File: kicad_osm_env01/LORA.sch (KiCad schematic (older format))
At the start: 12 parts

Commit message: kicad review sch initial
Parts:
- added TP?: Test_Point, TestPoint:TestPoint_THTPad_D1.0mm_Drill0.5mm, symbol OSM_env01-rescue:Test_Point-Connector-ESP32-EVB_Rev_D-rescue
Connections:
- net LORA_NRST: now reaches U?.18 (MCU_NRST)
- net LORA_NRST: now also TP?.1
- no-connect marks 14 -> 13
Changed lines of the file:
@@
 $Descr A4 11693 8268
 encoding utf-8
-Sheet 4 9
+Sheet 3 9
 Title ""
 Date ""
@@
 $EndComp
 Wire Wire Line
-	3300 3425 2950 3425
+	3300 3425 3250 3425
 Wire Wire Line
 	3300 3650 2950 3650
@@
 Text Label 2950 3650 0    50   ~ 0
 LORA_RX
-Text Label 2950 3425 0    50   ~ 0
-LORA_CTS
 Wire Wire Line
 	4000 2800 4275 2800
@@
 NoConn ~ 9025 3550
 NoConn ~ 9025 3425
-NoConn ~ 9025 3300
 NoConn ~ 7275 3550
 $Comp
@@
 Wire Wire Line
 	7275 3675 6900 3675
-Text Label 6900 3675 0    50   ~ 0
+Wire Wire Line
+	7275 3800 6900 3800
+Text HLabel 6900 3675 0    50   Input ~ 0
 LORA_RX
-Wire Wire Line
-	7275 3800 6900 3800
-Text Label 6900 3800 0    50   ~ 0
+Text HLabel 6900 3800 0    50   Input ~ 0
 LORA_TX
+Text HLabel 3175 3350 0    50   Input ~ 0
+LORA_CTS
+Wire Wire Line
+	3175 3350 3250 3350
+Wire Wire Line
+	3250 3350 3250 3425
+Connection ~ 3250 3425
+Wire Wire Line
+	3250 3425 2950 3425
+Text HLabel 9400 3300 2    50   Input ~ 0
+LORA_NRST
+Wire Wire Line
+	9400 3300 9300 3300
+$Comp
+L OSM_env01-rescue:Test_Point-Connector-ESP32-EVB_Rev_D-rescue TP?
+U 1 1 606B4551
+P 9300 3400
+AR Path="/606B4551" Ref="TP?"  Part="1"
+AR Path="/60880AD8/606B4551" Ref="TP?"  Part="1"
+F 0 "TP?" V 9300 4150 50  0000 C CNN
+F 1 "Test_Point" V 9300 3775 50  0000 C CNN
+F 2 "TestPoint:TestPoint_THTPad_D1.0mm_Drill0.5mm" H 9500 3400 50  0001 C CNN
+F 3 "~" H 9500 3400 50  0001 C CNN
+	1    9300 3400
+	0    1    -1   0
+$EndComp
+Wire Wire Line
+	9300 3400 9300 3300
+Connection ~ 9300 3300
+Wire Wire Line
+	9300 3300 9025 3300
 $EndSCHEMATC

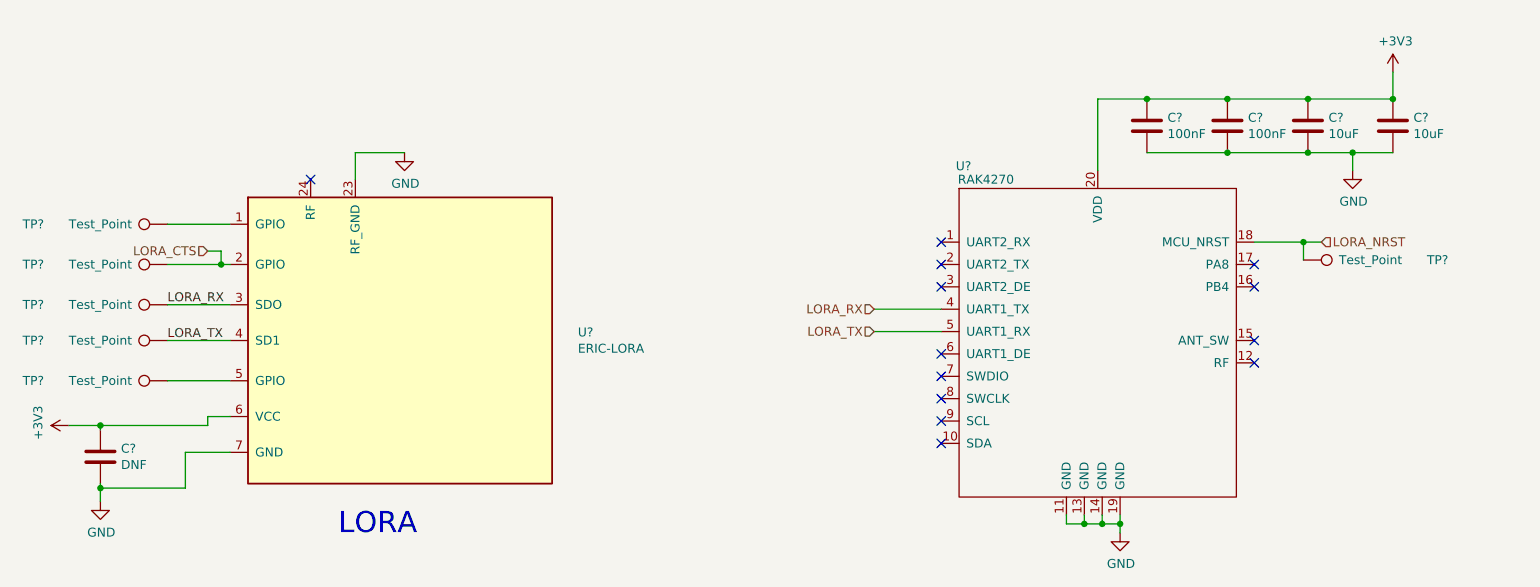
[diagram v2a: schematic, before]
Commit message: updated schematics
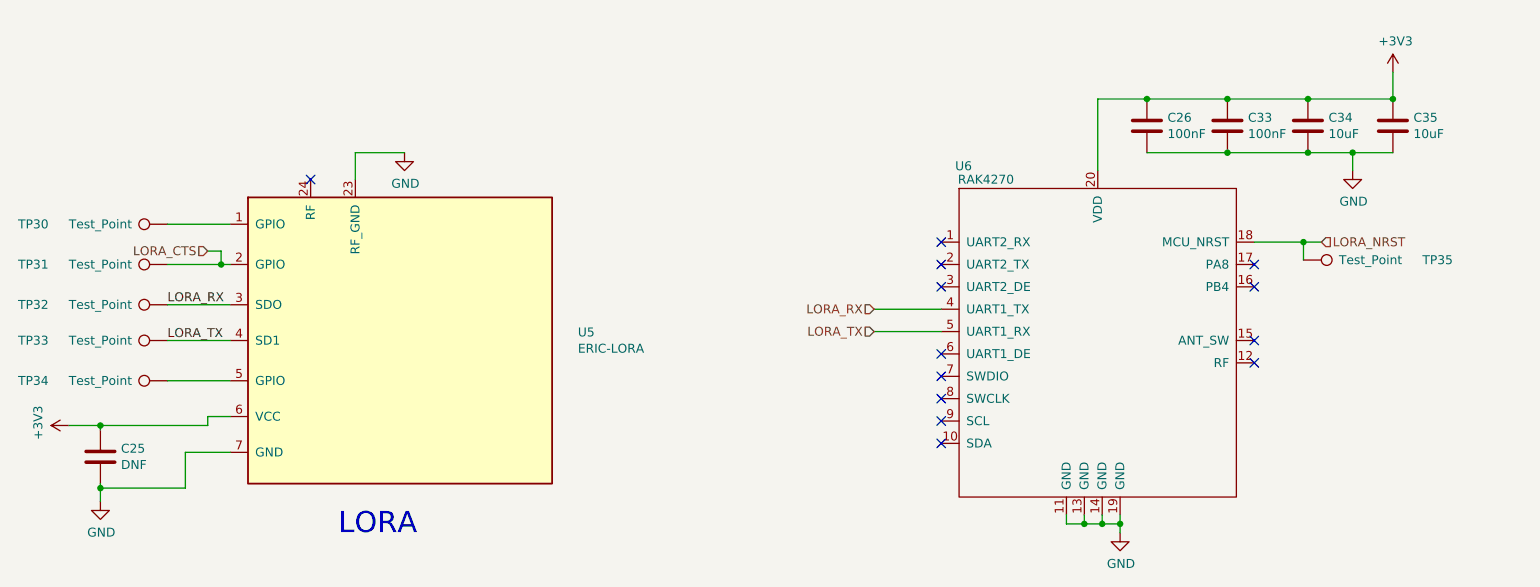
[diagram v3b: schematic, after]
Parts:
- gave numbers to parts that had none: 13
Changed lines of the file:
@@
 $Descr A4 11693 8268
 encoding utf-8
-Sheet 3 9
+Sheet 3 11
 Title ""
 Date ""
@@
 P 4200 3850
 AR Path="/608A2EA3" Ref="U?"  Part="1"
-AR Path="/60880AD8/608A2EA3" Ref="U?"  Part="1"
-F 0 "U?" H 5244 3896 50  0000 L CNN
+AR Path="/60880AD8/608A2EA3" Ref="U5"  Part="1"
+F 0 "U5" H 5244 3896 50  0000 L CNN
 F 1 "ERIC-LORA" H 5244 3805 50  0000 L CNN
 F 2 "Devtank_PCB_lib:eRIC-LoRa_RF_Module" H 4250 3000 50  0001 C CNN
@@
 P 4275 2800
 AR Path="/608A2EB0" Ref="#PWR?"  Part="1"
-AR Path="/60880AD8/608A2EB0" Ref="#PWR?"  Part="1"
-F 0 "#PWR?" H 4275 2550 50  0001 C CNN
+AR Path="/60880AD8/608A2EB0" Ref="#PWR050"  Part="1"
+F 0 "#PWR050" H 4275 2550 50  0001 C CNN
 F 1 "GND" H 4280 2627 50  0000 C CNN
 F 2 "" H 4275 2800 60  0000 C CNN
@@
 P 2950 3425
 AR Path="/608A2EB8" Ref="TP?"  Part="1"
-AR Path="/60880AD8/608A2EB8" Ref="TP?"  Part="1"
-F 0 "TP?" V 2950 4175 50  0000 C CNN
+AR Path="/60880AD8/608A2EB8" Ref="TP31"  Part="1"
+F 0 "TP31" V 2950 4175 50  0000 C CNN
 F 1 "Test_Point" V 2950 3800 50  0000 C CNN
 F 2 "TestPoint:TestPoint_THTPad_D1.0mm_Drill0.5mm" H 3150 3425 50  0001 C CNN
@@
 P 2950 3650
 AR Path="/608A2EBE" Ref="TP?"  Part="1"
-AR Path="/60880AD8/608A2EBE" Ref="TP?"  Part="1"
-F 0 "TP?" V 2950 4400 50  0000 C CNN
+AR Path="/60880AD8/608A2EBE" Ref="TP32"  Part="1"
+F 0 "TP32" V 2950 4400 50  0000 C CNN
 F 1 "Test_Point" V 2950 4025 50  0000 C CNN
 F 2 "TestPoint:TestPoint_THTPad_D1.0mm_Drill0.5mm" H 3150 3650 50  0001 C CNN
@@
 P 2950 3850
 AR Path="/608A2EC4" Ref="TP?"  Part="1"
-AR Path="/60880AD8/608A2EC4" Ref="TP?"  Part="1"
-F 0 "TP?" V 2950 4600 50  0000 C CNN
+AR Path="/60880AD8/608A2EC4" Ref="TP33"  Part="1"
+F 0 "TP33" V 2950 4600 50  0000 C CNN
 F 1 "Test_Point" V 2950 4225 50  0000 C CNN
 F 2 "TestPoint:TestPoint_THTPad_D1.0mm_Drill0.5mm" H 3150 3850 50  0001 C CNN
@@
 P 2950 3200
 AR Path="/608A2ECB" Ref="TP?"  Part="1"
-AR Path="/60880AD8/608A2ECB" Ref="TP?"  Part="1"
-F 0 "TP?" V 2950 3950 50  0000 C CNN
+AR Path="/60880AD8/608A2ECB" Ref="TP30"  Part="1"
+F 0 "TP30" V 2950 3950 50  0000 C CNN
 F 1 "Test_Point" V 2950 3575 50  0000 C CNN
 F 2 "TestPoint:TestPoint_THTPad_D1.0mm_Drill0.5mm" H 3150 3200 50  0001 C CNN
@@
 P 2950 4075
 AR Path="/608A2ED2" Ref="TP?"  Part="1"
-AR Path="/60880AD8/608A2ED2" Ref="TP?"  Part="1"
-F 0 "TP?" V 2950 4825 50  0000 C CNN
+AR Path="/60880AD8/608A2ED2" Ref="TP34"  Part="1"
+F 0 "TP34" V 2950 4825 50  0000 C CNN
 F 1 "Test_Point" V 2950 4450 50  0000 C CNN
 F 2 "TestPoint:TestPoint_THTPad_D1.0mm_Drill0.5mm" H 3150 4075 50  0001 C CNN
@@
 P 2575 4500
 AR Path="/608A2ED9" Ref="C?"  Part="1"
-AR Path="/60880AD8/608A2ED9" Ref="C?"  Part="1"
-F 0 "C?" H 2690 4546 50  0000 L CNN
+AR Path="/60880AD8/608A2ED9" Ref="C25"  Part="1"
+F 0 "C25" H 2690 4546 50  0000 L CNN
 F 1 "DNF" H 2690 4455 50  0000 L CNN
 F 2 "Capacitor_SMD:C_0402_1005Metric" H 2613 4350 50  0001 C CNN
@@
 P 2575 4750
 AR Path="/608A2EDF" Ref="#PWR?"  Part="1"
-AR Path="/60880AD8/608A2EDF" Ref="#PWR?"  Part="1"
-F 0 "#PWR?" H 2575 4500 50  0001 C CNN
+AR Path="/60880AD8/608A2EDF" Ref="#PWR049"  Part="1"
+F 0 "#PWR049" H 2575 4500 50  0001 C CNN
 F 1 "GND" H 2580 4577 50  0000 C CNN
 F 2 "" H 2575 4750 60  0000 C CNN
@@
 P 2400 4325
 AR Path="/608A2EE5" Ref="#PWR?"  Part="1"
-AR Path="/60880AD8/608A2EE5" Ref="#PWR?"  Part="1"
-F 0 "#PWR?" H 2400 4175 50  0001 C CNN
+AR Path="/60880AD8/608A2EE5" Ref="#PWR048"  Part="1"
+F 0 "#PWR048" H 2400 4175 50  0001 C CNN
 F 1 "+3V3" H 2415 4498 50  0000 C CNN
 F 2 "" H 2400 4325 50  0001 C CNN
@@
 P 8425 2650
 AR Path="/608CFA0F" Ref="C?"  Part="1"
-AR Path="/60880AD8/608CFA0F" Ref="C?"  Part="1"
-F 0 "C?" H 8540 2696 50  0000 L CNN
+AR Path="/60880AD8/608CFA0F" Ref="C26"  Part="1"
+F 0 "C26" H 8540 2696 50  0000 L CNN
 F 1 "100nF" H 8540 2605 50  0000 L CNN
 F 2 "" H 8463 2500 50  0001 C CNN
@@
 P 8875 2650
 AR Path="/608CFA15" Ref="C?"  Part="1"
-AR Path="/60880AD8/608CFA15" Ref="C?"  Part="1"
-F 0 "C?" H 8990 2696 50  0000 L CNN
+AR Path="/60880AD8/608CFA15" Ref="C33"  Part="1"
+F 0 "C33" H 8990 2696 50  0000 L CNN
 F 1 "100nF" H 8990 2605 50  0000 L CNN
 F 2 "" H 8913 2500 50  0001 C CNN
@@
 P 9325 2650
 AR Path="/608CFA1B" Ref="C?"  Part="1"
-AR Path="/60880AD8/608CFA1B" Ref="C?"  Part="1"
-F 0 "C?" H 9440 2696 50  0000 L CNN
+AR Path="/60880AD8/608CFA1B" Ref="C34"  Part="1"
+F 0 "C34" H 9440 2696 50  0000 L CNN
 F 1 "10uF" H 9440 2605 50  0000 L CNN
 F 2 "" H 9363 2500 50  0001 C CNN
@@
 P 9800 2650
 AR Path="/608CFA21" Ref="C?"  Part="1"
-AR Path="/60880AD8/608CFA21" Ref="C?"  Part="1"
-F 0 "C?" H 9915 2696 50  0000 L CNN
+AR Path="/60880AD8/608CFA21" Ref="C35"  Part="1"
+F 0 "C35" H 9915 2696 50  0000 L CNN
 F 1 "10uF" H 9915 2605 50  0000 L CNN
 F 2 "" H 9838 2500 50  0001 C CNN
@@
 P 9575 2900
 AR Path="/608CFA34" Ref="#PWR?"  Part="1"
-AR Path="/60880AD8/608CFA34" Ref="#PWR?"  Part="1"
-F 0 "#PWR?" H 9575 2650 50  0001 C CNN
+AR Path="/60880AD8/608CFA34" Ref="#PWR052"  Part="1"
+F 0 "#PWR052" H 9575 2650 50  0001 C CNN
 F 1 "GND" H 9580 2727 50  0000 C CNN
 F 2 "" H 9575 2900 60  0000 C CNN
@@
 P 8275 4925
 AR Path="/608CFA3D" Ref="#PWR?"  Part="1"
-AR Path="/60880AD8/608CFA3D" Ref="#PWR?"  Part="1"
-F 0 "#PWR?" H 8275 4675 50  0001 C CNN
+AR Path="/60880AD8/608CFA3D" Ref="#PWR051"  Part="1"
+F 0 "#PWR051" H 8275 4675 50  0001 C CNN
 F 1 "GND" H 8280 4752 50  0000 C CNN
 F 2 "" H 8275 4925 60  0000 C CNN
@@
 P 9800 2350
 AR Path="/608CFA4E" Ref="#PWR?"  Part="1"
-AR Path="/60880AD8/608CFA4E" Ref="#PWR?"  Part="1"
-F 0 "#PWR?" H 9800 2200 50  0001 C CNN
+AR Path="/60880AD8/608CFA4E" Ref="#PWR053"  Part="1"
+F 0 "#PWR053" H 9800 2200 50  0001 C CNN
 F 1 "+3V3" H 9815 2523 50  0000 C CNN
 F 2 "" H 9800 2350 50  0001 C CNN
@@
 P 8150 3800
 AR Path="/608CFA5C" Ref="U?"  Part="1"
-AR Path="/60880AD8/608CFA5C" Ref="U?"  Part="1"
-F 0 "U?" H 7400 4725 50  0000 C CNN
+AR Path="/60880AD8/608CFA5C" Ref="U6"  Part="1"
+F 0 "U6" H 7400 4725 50  0000 C CNN
 F 1 "RAK4270" H 7525 4650 50  0000 C CNN
 F 2 "" H 7900 4175 50  0001 C CNN
@@
 P 9300 3400
 AR Path="/606B4551" Ref="TP?"  Part="1"
-AR Path="/60880AD8/606B4551" Ref="TP?"  Part="1"
-F 0 "TP?" V 9300 4150 50  0000 C CNN
+AR Path="/60880AD8/606B4551" Ref="TP35"  Part="1"
+F 0 "TP35" V 9300 4150 50  0000 C CNN
 F 1 "Test_Point" V 9300 3775 50  0000 C CNN
 F 2 "TestPoint:TestPoint_THTPad_D1.0mm_Drill0.5mm" H 9500 3400 50  0001 C CNN

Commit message: schematics awaiting review
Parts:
- added C70: 100nF, symbol device:C
- added R123: 10k, symbol device:R
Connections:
- net +3V3: now also R123.1
- net GND: now also C70.2
- net LORA_NRST: now also C70.1, R123.2
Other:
- moved on the sheet: C26, C33, C34, C35
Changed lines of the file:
@@
 AR Path="/608A2EA3" Ref="U?"  Part="1"
 AR Path="/60880AD8/608A2EA3" Ref="U5"  Part="1"
-F 0 "U5" H 5244 3896 50  0000 L CNN
-F 1 "ERIC-LORA" H 5244 3805 50  0000 L CNN
+F 0 "U5" H 4700 4825 50  0000 L CNN
+F 1 "ERIC-LORA" H 4700 4725 50  0000 L CNN
 F 2 "Devtank_PCB_lib:eRIC-LoRa_RF_Module" H 4250 3000 50  0001 C CNN
 F 3 "http://www.wireless-solutions.de/images/stories/downloads/Radio%20Modules/iM880A/General_Information/iM880A_Datasheet_V1_1.pdf" H 4250 3000 50  0001 C CNN
@@
 AR Path="/608A2EB8" Ref="TP?"  Part="1"
 AR Path="/60880AD8/608A2EB8" Ref="TP31"  Part="1"
-F 0 "TP31" V 2950 4175 50  0000 C CNN
-F 1 "Test_Point" V 2950 3800 50  0000 C CNN
+F 0 "TP31" V 2950 3700 50  0000 C CNN
+F 1 "Test_Point" V 2950 3800 50  0001 C CNN
 F 2 "TestPoint:TestPoint_THTPad_D1.0mm_Drill0.5mm" H 3150 3425 50  0001 C CNN
 F 3 "~" H 3150 3425 50  0001 C CNN
@@
 AR Path="/608A2EBE" Ref="TP?"  Part="1"
 AR Path="/60880AD8/608A2EBE" Ref="TP32"  Part="1"
-F 0 "TP32" V 2950 4400 50  0000 C CNN
-F 1 "Test_Point" V 2950 4025 50  0000 C CNN
+F 0 "TP32" V 2950 3925 50  0000 C CNN
+F 1 "Test_Point" V 2950 4025 50  0001 C CNN
 F 2 "TestPoint:TestPoint_THTPad_D1.0mm_Drill0.5mm" H 3150 3650 50  0001 C CNN
 F 3 "~" H 3150 3650 50  0001 C CNN
@@
 AR Path="/608A2EC4" Ref="TP?"  Part="1"
 AR Path="/60880AD8/608A2EC4" Ref="TP33"  Part="1"
-F 0 "TP33" V 2950 4600 50  0000 C CNN
-F 1 "Test_Point" V 2950 4225 50  0000 C CNN
+F 0 "TP33" V 2950 4125 50  0000 C CNN
+F 1 "Test_Point" V 2950 4225 50  0001 C CNN
 F 2 "TestPoint:TestPoint_THTPad_D1.0mm_Drill0.5mm" H 3150 3850 50  0001 C CNN
 F 3 "~" H 3150 3850 50  0001 C CNN
@@
 AR Path="/608A2ECB" Ref="TP?"  Part="1"
 AR Path="/60880AD8/608A2ECB" Ref="TP30"  Part="1"
-F 0 "TP30" V 2950 3950 50  0000 C CNN
-F 1 "Test_Point" V 2950 3575 50  0000 C CNN
+F 0 "TP30" V 2950 3475 50  0000 C CNN
+F 1 "Test_Point" V 2950 3575 50  0001 C CNN
 F 2 "TestPoint:TestPoint_THTPad_D1.0mm_Drill0.5mm" H 3150 3200 50  0001 C CNN
 F 3 "~" H 3150 3200 50  0001 C CNN
@@
 AR Path="/608A2ED2" Ref="TP?"  Part="1"
 AR Path="/60880AD8/608A2ED2" Ref="TP34"  Part="1"
-F 0 "TP34" V 2950 4825 50  0000 C CNN
-F 1 "Test_Point" V 2950 4450 50  0000 C CNN
+F 0 "TP34" V 2950 4350 50  0000 C CNN
+F 1 "Test_Point" V 2950 4450 50  0001 C CNN
 F 2 "TestPoint:TestPoint_THTPad_D1.0mm_Drill0.5mm" H 3150 4075 50  0001 C CNN
 F 3 "~" H 3150 4075 50  0001 C CNN
@@
 L device:C C?
 U 1 1 608CFA0F
-P 8425 2650
+P 7850 2550
 AR Path="/608CFA0F" Ref="C?"  Part="1"
 AR Path="/60880AD8/608CFA0F" Ref="C26"  Part="1"
-F 0 "C26" H 8540 2696 50  0000 L CNN
-F 1 "100nF" H 8540 2605 50  0000 L CNN
-F 2 "" H 8463 2500 50  0001 C CNN
-F 3 "" H 8425 2650 50  0001 C CNN
-	1    8425 2650
-	1    0    0    -1
+F 0 "C26" H 7965 2596 50  0000 L CNN
+F 1 "100nF" H 7965 2505 50  0000 L CNN
+F 2 "" H 7888 2400 50  0001 C CNN
+F 3 "" H 7850 2550 50  0001 C CNN
+	1    7850 2550
+	-1   0    0    -1
 $EndComp
 $Comp
 L device:C C?
 U 1 1 608CFA15
-P 8875 2650
+P 7400 2550
 AR Path="/608CFA15" Ref="C?"  Part="1"
 AR Path="/60880AD8/608CFA15" Ref="C33"  Part="1"
-F 0 "C33" H 8990 2696 50  0000 L CNN
-F 1 "100nF" H 8990 2605 50  0000 L CNN
-F 2 "" H 8913 2500 50  0001 C CNN
-F 3 "" H 8875 2650 50  0001 C CNN
-	1    8875 2650
-	1    0    0    -1
+F 0 "C33" H 7515 2596 50  0000 L CNN
+F 1 "100nF" H 7515 2505 50  0000 L CNN
+F 2 "" H 7438 2400 50  0001 C CNN
+F 3 "" H 7400 2550 50  0001 C CNN
+	1    7400 2550
+	-1   0    0    -1
 $EndComp
 $Comp
 L device:C C?
 U 1 1 608CFA1B
-P 9325 2650
+P 6950 2550
 AR Path="/608CFA1B" Ref="C?"  Part="1"
 AR Path="/60880AD8/608CFA1B" Ref="C34"  Part="1"
-F 0 "C34" H 9440 2696 50  0000 L CNN
-F 1 "10uF" H 9440 2605 50  0000 L CNN
-F 2 "" H 9363 2500 50  0001 C CNN
-F 3 "" H 9325 2650 50  0001 C CNN
-	1    9325 2650
-	1    0    0    -1
+F 0 "C34" H 7065 2596 50  0000 L CNN
+F 1 "10uF" H 7065 2505 50  0000 L CNN
+F 2 "" H 6988 2400 50  0001 C CNN
+F 3 "" H 6950 2550 50  0001 C CNN
+	1    6950 2550
+	-1   0    0    -1
 $EndComp
 $Comp
 L device:C C?
 U 1 1 608CFA21
-P 9800 2650
+P 6475 2550
 AR Path="/608CFA21" Ref="C?"  Part="1"
 AR Path="/60880AD8/608CFA21" Ref="C35"  Part="1"
-F 0 "C35" H 9915 2696 50  0000 L CNN
-F 1 "10uF" H 9915 2605 50  0000 L CNN
-F 2 "" H 9838 2500 50  0001 C CNN
-F 3 "" H 9800 2650 50  0001 C CNN
-	1    9800 2650
-	1    0    0    -1
-$EndComp
-Wire Wire Line
-	8150 2900 8150 2500
-Wire Wire Line
-	8150 2500 8425 2500
-Connection ~ 8425 2500
-Wire Wire Line
-	8425 2500 8875 2500
-Connection ~ 8875 2500
-Wire Wire Line
-	8875 2500 9325 2500
-Connection ~ 9325 2500
-Wire Wire Line
-	9325 2500 9800 2500
-Wire Wire Line
-	8425 2800 8875 2800
-Connection ~ 8875 2800
-Wire Wire Line
-	8875 2800 9325 2800
-Connection ~ 9325 2800
-Wire Wire Line
-	9325 2800 9575 2800
+F 0 "C35" H 6590 2596 50  0000 L CNN
+F 1 "10uF" H 6590 2505 50  0000 L CNN
+F 2 "" H 6513 2400 50  0001 C CNN
+F 3 "" H 6475 2550 50  0001 C CNN
+	1    6475 2550
+	-1   0    0    -1
+$EndComp
+Connection ~ 7850 2400
+Wire Wire Line
+	7850 2400 7400 2400
+Connection ~ 7400 2400
+Wire Wire Line
+	7400 2400 6950 2400
+Connection ~ 6950 2400
+Wire Wire Line
+	6950 2400 6475 2400
+Wire Wire Line
+	7850 2700 7400 2700
+Connection ~ 7400 2700
+Wire Wire Line
+	7400 2700 6950 2700
+Connection ~ 6950 2700
+Wire Wire Line
+	6950 2700 6700 2700
 $Comp
 L OSM_env01:GND #PWR?
 U 1 1 608CFA34
-P 9575 2900
+P 6700 2800
 AR Path="/608CFA34" Ref="#PWR?"  Part="1"
 AR Path="/60880AD8/608CFA34" Ref="#PWR052"  Part="1"
-F 0 "#PWR052" H 9575 2650 50  0001 C CNN
-F 1 "GND" H 9580 2727 50  0000 C CNN
-F 2 "" H 9575 2900 60  0000 C CNN
-F 3 "" H 9575 2900 60  0000 C CNN
-	1    9575 2900
-	1    0    0    -1
-$EndComp
-Wire Wire Line
-	9575 2900 9575 2800
-Connection ~ 9575 2800
-Wire Wire Line
-	9575 2800 9800 2800
+F 0 "#PWR052" H 6700 2550 50  0001 C CNN
+F 1 "GND" H 6705 2627 50  0000 C CNN
+F 2 "" H 6700 2800 60  0000 C CNN
+F 3 "" H 6700 2800 60  0000 C CNN
+	1    6700 2800
+	-1   0    0    -1
+$EndComp
+Wire Wire Line
+	6700 2800 6700 2700
+Connection ~ 6700 2700
+Wire Wire Line
+	6700 2700 6475 2700
 $Comp
 L OSM_env01:GND #PWR?
@@
 L power:+3V3 #PWR?
 U 1 1 608CFA4E
-P 9800 2350
+P 6475 2250
 AR Path="/608CFA4E" Ref="#PWR?"  Part="1"
 AR Path="/60880AD8/608CFA4E" Ref="#PWR053"  Part="1"
-F 0 "#PWR053" H 9800 2200 50  0001 C CNN
-F 1 "+3V3" H 9815 2523 50  0000 C CNN
-F 2 "" H 9800 2350 50  0001 C CNN
-F 3 "" H 9800 2350 50  0001 C CNN
-	1    9800 2350
-	1    0    0    -1
-$EndComp
-Wire Wire Line
-	9800 2500 9800 2350
-Connection ~ 9800 2500
+F 0 "#PWR053" H 6475 2100 50  0001 C CNN
+F 1 "+3V3" H 6490 2423 50  0000 C CNN
+F 2 "" H 6475 2250 50  0001 C CNN
+F 3 "" H 6475 2250 50  0001 C CNN
+	1    6475 2250
+	1    0    0    -1
+$EndComp
+Wire Wire Line
+	6475 2400 6475 2250
+Connection ~ 6475 2400
 NoConn ~ 9025 3975
 NoConn ~ 9025 3850
@@
 AR Path="/608CFA5C" Ref="U?"  Part="1"
 AR Path="/60880AD8/608CFA5C" Ref="U6"  Part="1"
-F 0 "U6" H 7400 4725 50  0000 C CNN
-F 1 "RAK4270" H 7525 4650 50  0000 C CNN
+F 0 "U6" H 8625 4750 50  0000 C CNN
+F 1 "RAK4270" H 8750 4650 50  0000 C CNN
 F 2 "" H 7900 4175 50  0001 C CNN
 F 3 "" H 7900 4175 50  0001 C CNN
@@
 Wire Wire Line
 	3250 3425 2950 3425
-Text HLabel 9400 3300 2    50   Input ~ 0
+Text HLabel 10000 3300 2    50   Input ~ 0
 LORA_NRST
-Wire Wire Line
-	9400 3300 9300 3300
-$Comp
-L OSM_env01-rescue:Test_Point-Connector-ESP32-EVB_Rev_D-rescue TP?
-U 1 1 606B4551
-P 9300 3400
-AR Path="/606B4551" Ref="TP?"  Part="1"
-AR Path="/60880AD8/606B4551" Ref="TP35"  Part="1"
-F 0 "TP35" V 9300 4150 50  0000 C CNN
-F 1 "Test_Point" V 9300 3775 50  0000 C CNN
-F 2 "TestPoint:TestPoint_THTPad_D1.0mm_Drill0.5mm" H 9500 3400 50  0001 C CNN
-F 3 "~" H 9500 3400 50  0001 C CNN
-	1    9300 3400
-	0    1    -1   0
-$EndComp
-Wire Wire Line
-	9300 3400 9300 3300
-Connection ~ 9300 3300
-Wire Wire Line
-	9300 3300 9025 3300
+$Comp
+L device:R R123
+U 1 1 606EC59D
+P 9575 3100
+F 0 "R123" H 9645 3146 50  0000 L CNN
+F 1 "10k" H 9645 3055 50  0000 L CNN
+F 2 "" V 9505 3100 50  0001 C CNN
+F 3 "" H 9575 3100 50  0001 C CNN
+	1    9575 3100
+	1    0    0    -1
+$EndComp
+$Comp
+L device:C C70
+U 1 1 606EC843
+P 9575 3525
+F 0 "C70" H 9690 3571 50  0000 L CNN
+F 1 "100nF" H 9690 3480 50  0000 L CNN
+F 2 "" H 9613 3375 50  0001 C CNN
+F 3 "" H 9575 3525 50  0001 C CNN
+	1    9575 3525
+	1    0    0    -1
+$EndComp
+$Comp
+L power:GND #PWR0129
+U 1 1 606F28DC
+P 9575 3800
+F 0 "#PWR0129" H 9575 3550 50  0001 C CNN
+F 1 "GND" H 9580 3627 50  0000 C CNN
+F 2 "" H 9575 3800 50  0001 C CNN
+F 3 "" H 9575 3800 50  0001 C CNN
+	1    9575 3800
+	1    0    0    -1
+$EndComp
+Wire Wire Line
+	9575 3675 9575 3800
+Wire Wire Line
+	9575 3375 9575 3300
+Connection ~ 9575 3300
+Wire Wire Line
+	9575 3300 9575 3250
+$Comp
+L power:+3V3 #PWR0130
+U 1 1 60700EDF
+P 9575 2850
+F 0 "#PWR0130" H 9575 2700 50  0001 C CNN
+F 1 "+3V3" H 9590 3023 50  0000 C CNN
+F 2 "" H 9575 2850 50  0001 C CNN
+F 3 "" H 9575 2850 50  0001 C CNN
+	1    9575 2850
+	1    0    0    -1
+$EndComp
+Wire Wire Line
+	8150 2900 8150 2400
+Wire Wire Line
+	7850 2400 8150 2400
+Wire Wire Line
+	9025 3300 9575 3300
+Wire Wire Line
+	9575 2950 9575 2850
+Wire Wire Line
+	9575 3300 9900 3300
+Wire Wire Line
+	9900 3400 9900 3300
+Connection ~ 9900 3300
+Wire Wire Line
+	9900 3300 10000 3300
+$Comp
+L OSM_env01-rescue:Test_Point-Connector-ESP32-EVB_Rev_D-rescue TP?
+U 1 1 60A76064
+P 9900 3400
+AR Path="/5F6F7717/60A76064" Ref="TP?"  Part="1"
+AR Path="/60A76064" Ref="TP?"  Part="1"
+AR Path="/608F4675/60A76064" Ref="TP?"  Part="1"
+AR Path="/60880AD8/60A76064" Ref="TP35"  Part="1"
+F 0 "TP35" V 9900 3675 50  0000 C CNN
+F 1 "Test_Point" V 9975 3625 50  0001 C CNN
+F 2 "TestPoint:TestPoint_THTPad_D1.0mm_Drill0.5mm" H 10100 3400 50  0001 C CNN
+F 3 "~" H 10100 3400 50  0001 C CNN
+	1    9900 3400
+	0    1    1    0
+$EndComp
 $EndSCHEMATC
